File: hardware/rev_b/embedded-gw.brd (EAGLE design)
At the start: 38.5 x 55.5 mm, 57 parts, among them J1 DM3BT-DSF-PEJS, J2 TC2030-JLINK-NL, J3 USB-A-MALE-PLUG, Q1 DMN32D2LDF, U1 AP7362A-33SP-13, U2 BT840X, U3 CP2102N-20, U4 ESDR0502N, U5 ESP32-WROVER-E, U6 ESP32-WROVER-E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

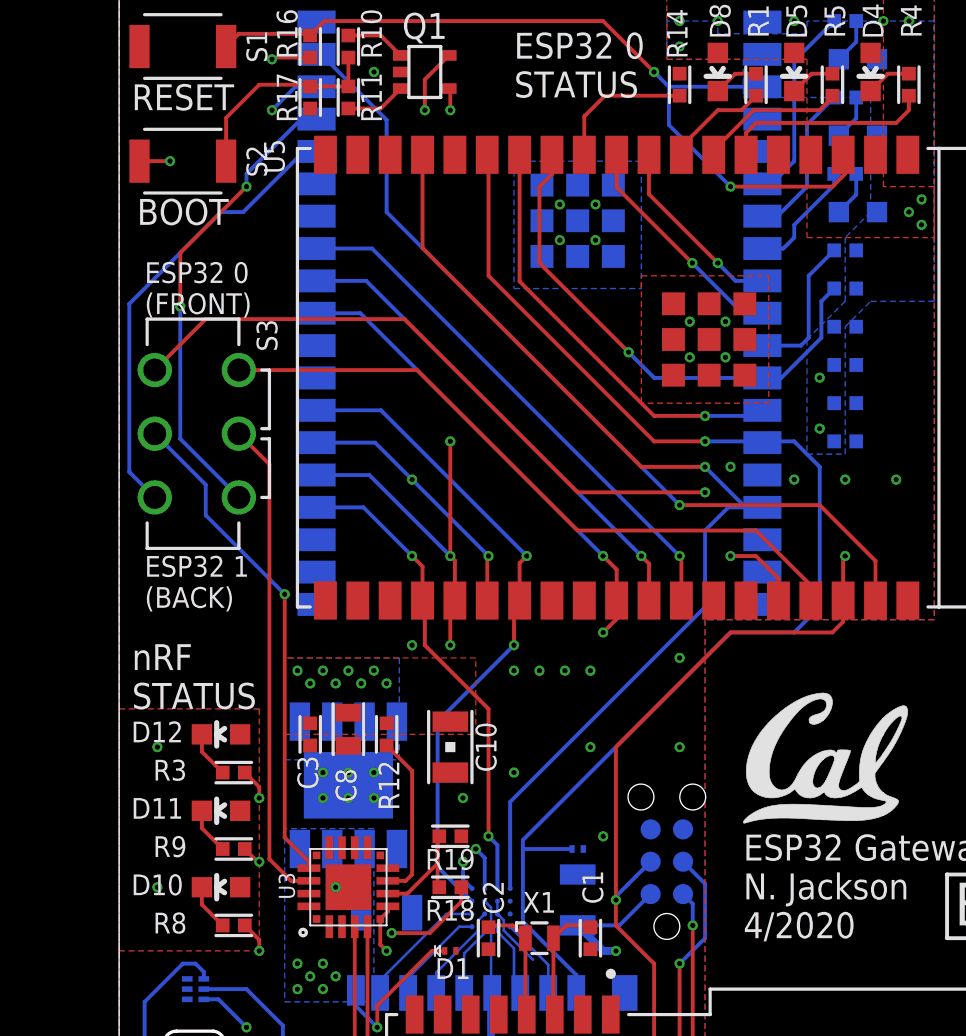
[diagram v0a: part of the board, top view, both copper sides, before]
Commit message: Change handshake gpio from 33 to 21, add ipc
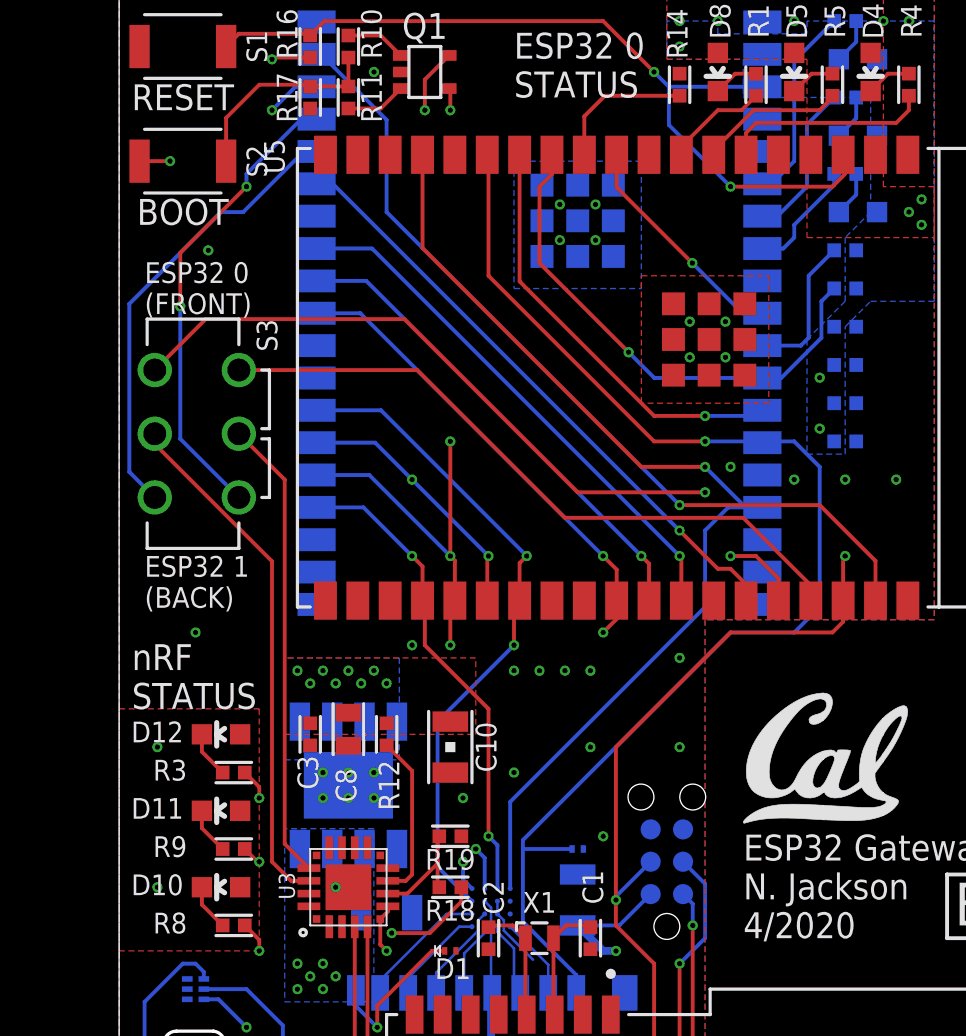
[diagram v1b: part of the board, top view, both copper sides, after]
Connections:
- net ESP32_HANDSHAKE: now also U5.33, U6.33; no longer U5.9, U6.9
- net RXD: now also U3.18; no longer U3.17
- net TXD: now also U3.17; no longer U3.18
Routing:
- net ESP32_HANDSHAKE: track 7.41 -> 24.0 mm
- net RXD: track 19.6 -> 20.5 mm, vias 1 -> 0
- net TXD: track 19.1 -> 18.2 mm
- net GND: vias 41 -> 43
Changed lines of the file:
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@@
 <param name="tpViaShape" value="round"/>
 <param name="PrefDir.1" value="-"/>
-<param name="PrefDir.2" value="*"/>
+<param name="PrefDir.2" value="0"/>
 <param name="PrefDir.3" value="0"/>
 <param name="PrefDir.4" value="0"/>
@@
 <via x="16.5" y="13.5" extent="1-16" drill="0.2032"/>
 <contactref element="R19" pad="1"/>
+<via x="3" y="30.5" extent="1-16" drill="0.2032"/>
+<via x="3.5" y="45.5" extent="1-16" drill="0.2032"/>
 </signal>
 <signal name="VCC">
@@
 </signal>
 <signal name="RXD">
+<contactref element="S3" pad="2"/>
+<contactref element="U3" pad="18"/>
+<wire x1="1.4" y1="38.3" x2="1.4" y2="37.89395625" width="0.1524" layer="1"/>
+<wire x1="6" y1="33.29395625" x2="1.4" y2="37.89395625" width="0.1524" layer="1"/>
+<wire x1="6.75" y1="20.75" x2="7.45" y2="20.75" width="0.1524" layer="1"/>
+<wire x1="6" y1="33.29395625" x2="6" y2="21.5" width="0.1524" layer="1"/>
+<wire x1="6" y1="21.5" x2="6.75" y2="20.75" width="0.1524" layer="1"/>
+</signal>
+<signal name="TXD">
+<contactref element="S3" pad="5"/>
+<wire x1="6.5" y1="36.5" x2="4.7" y2="38.3" width="0.1524" layer="1"/>
 <contactref element="U3" pad="17"/>
-<contactref element="S3" pad="2"/>
-<wire x1="7.45" y1="21.25" x2="7.45" y2="21.49855" width="0.1524" layer="1"/>
-<wire x1="7.45" y1="21.49855" x2="6.5" y2="22.44855" width="0.1524" layer="1"/>
-<wire x1="6.5" y1="22.44855" x2="6.5" y2="32" width="0.1524" layer="1"/>
-<wire x1="1.4" y1="38.3" x2="3.4" y2="36.3" width="0.1524" layer="16"/>
-<wire x1="6.5" y1="32" x2="3.4" y2="35.1" width="0.1524" layer="16"/>
-<via x="6.5" y="32" extent="1-16" drill="0.2032"/>
-<wire x1="3.4" y1="36.3" x2="3.4" y2="35.1" width="0.1524" layer="16"/>
-</signal>
-<signal name="TXD">
-<contactref element="U3" pad="18"/>
-<contactref element="S3" pad="5"/>
-<wire x1="6.75" y1="20.75" x2="7.45" y2="20.75" width="0.1524" layer="1"/>
-<wire x1="6.75" y1="20.75" x2="5.9" y2="21.6" width="0.1524" layer="1"/>
-<wire x1="5.9" y1="37.1" x2="4.7" y2="38.3" width="0.1524" layer="1"/>
-<wire x1="5.9" y1="21.6" x2="5.9" y2="37.1" width="0.1524" layer="1"/>
+<wire x1="6.5" y1="36.5" x2="6.5" y2="22.2" width="0.1524" layer="1"/>
+<wire x1="7.45" y1="21.25" x2="6.5" y2="22.2" width="0.1524" layer="1"/>
 </signal>
 <signal name="ESP32_0_TXD">
@@
 <contactref element="U5" pad="35"/>
 <wire x1="27.15" y1="31.75" x2="27.15" y2="32.35" width="0.1524" layer="1"/>
-<wire x1="27.15" y1="32.35" x2="25" y2="34.5" width="0.1524" layer="1"/>
-<wire x1="25" y1="34.5" x2="18" y2="34.5" width="0.1524" layer="1"/>
+<wire x1="27.15" y1="32.35" x2="24.5" y2="35" width="0.1524" layer="1"/>
+<wire x1="24.5" y1="35" x2="17.5" y2="35" width="0.1524" layer="1"/>
 <wire x1="4.7" y1="40.8" x2="11.7" y2="40.8" width="0.1524" layer="1"/>
-<wire x1="11.7" y1="40.8" x2="18" y2="34.5" width="0.1524" layer="1"/>
+<wire x1="11.7" y1="40.8" x2="17.5" y2="35" width="0.1524" layer="1"/>
 </signal>
 <signal name="ESP32_1_TXD">
@@
 </signal>
 <signal name="ESP32_HANDSHAKE">
-<contactref element="U6" pad="9"/>
-<contactref element="U5" pad="9"/>
-<wire x1="20.8" y1="49.25" x2="20.8" y2="47.7" width="0.1524" layer="1"/>
-<wire x1="20.8" y1="47.7" x2="23.5" y2="45" width="0.1524" layer="1"/>
-<via x="23.5" y="45" extent="1-16" drill="0.2032"/>
-<wire x1="23.5" y1="45" x2="24.2" y2="44.3" width="0.1524" layer="16"/>
-<wire x1="24.2" y1="44.3" x2="25.25" y2="44.3" width="0.1524" layer="16"/>
+<contactref element="U5" pad="33"/>
+<contactref element="U6" pad="33"/>
+<wire x1="7.75" y1="48.11" x2="8.39" y2="48.11" width="0.1524" layer="16"/>
+<via x="22" y="34.5" extent="1-16" drill="0.2032"/>
+<wire x1="23.5" y1="33" x2="22" y2="34.5" width="0.1524" layer="1"/>
+<wire x1="8.39" y1="48.11" x2="22" y2="34.5" width="0.1524" layer="16"/>
+<wire x1="24.61" y1="31.75" x2="24.61" y2="32.39" width="0.1524" layer="1"/>
+<wire x1="24.61" y1="32.39" x2="24" y2="33" width="0.1524" layer="1"/>
+<wire x1="24" y1="33" x2="23.5" y2="33" width="0.1524" layer="1"/>
 </signal>
 <signal name="N$12">
